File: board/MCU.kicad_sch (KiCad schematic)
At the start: 20 parts, among them Q1 NMOS, U1 1EDL8011XUMA1, U7 ESP32-S2-DEVKITM-1U

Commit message: Add OpAmp link
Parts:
- removed Conn1: Molex_uF_D_10, MRDT_Connectors:MOLEX_uF_D_10_Horizontal, symbol MRDT_Connectors:Molex_uF_D_10
- added Conn5: Molex_SL_09, symbol MRDT_Connectors:Molex_SL_09
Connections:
- net +5V: now also Conn5.8
- net GND: now also Conn5.7
- net GPIO 10: now also Conn5.1
- net GPIO 4: now also Conn5.9
- net GPIO 5: now also Conn5.6
- net GPIO 6: now also Conn5.5
- net GPIO 7: now also Conn5.4
- net GPIO 8: now also Conn5.3
- net GPIO 9: now also Conn5.2
- no-connect marks 0 -> 1
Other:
- moved on the sheet: Q1
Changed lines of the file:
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@@
 	)
 	(junction
+		(at 123.19 180.34)
+		(diameter 0)
+		(color 0 0 0 0)
+	)
+	(junction
 		(at 123.19 139.7)
 		(diameter 0)
@@
 	)
 	(junction
-		(at 137.16 180.34)
-		(diameter 0)
-		(color 0 0 0 0)
-	)
-	(junction
 		(at 101.6 158.75)
 		(diameter 0)
@@
 		(color 0 0 0 0)
 	)
+	(no_connect
+		(at 157.48 130.81)
+	)
 	(wire
 		(pts
@@
 	(wire
 		(pts
-			(xy 137.16 168.91) (xy 137.16 139.7)
+			(xy 123.19 168.91) (xy 123.19 139.7)
 		)
 		(stroke
@@
 	(wire
 		(pts
-			(xy 101.6 173.99) (xy 129.54 173.99)
+			(xy 101.6 173.99) (xy 115.57 173.99)
 		)
 		(stroke
@@
 	(wire
 		(pts
-			(xy 114.3 180.34) (xy 137.16 180.34)
-		)
-		(stroke
-			(width 0)
-			(type default)
-		)
-	)
-	(wire
-		(pts
-			(xy 137.16 139.7) (xy 123.19 139.7)
+			(xy 114.3 180.34) (xy 123.19 180.34)
 		)
 		(stroke
@@
 	(wire
 		(pts
-			(xy 137.16 180.34) (xy 137.16 184.15)
+			(xy 123.19 180.34) (xy 123.19 184.15)
 		)
 		(stroke
@@
 	(wire
 		(pts
-			(xy 137.16 180.34) (xy 137.16 179.07)
+			(xy 123.19 180.34) (xy 123.19 179.07)
 		)
 		(stroke
@@
 	(wire
 		(pts
-			(xy 101.6 172.72) (xy 101.6 173.99)
+			(xy 101.6 173.99) (xy 101.6 172.72)
 		)
 		(stroke
@@
 	(global_label "ESC_PWR"
 		(shape output)
-		(at 137.16 184.15 270)
+		(at 123.19 184.15 270)
 		(fields_autoplaced yes)
 		(effects
@@
 		)
 		(property "Intersheetrefs" "${INTERSHEET_REFS}"
-			(at 137.16 195.7227 90)
+			(at 123.19 195.7227 90)
 			(effects
 				(font
@@
 	(symbol
 		(lib_id "Simulation_SPICE:NMOS")
-		(at 134.62 173.99 0)
+		(at 120.65 173.99 0)
 		(unit 1)
 		(exclude_from_sim no)
@@
 		(fields_autoplaced yes)
 		(property "Reference" "Q1"
-			(at 140.97 172.7199 0)
+			(at 127 172.7199 0)
 			(effects
 				(font
@@
 		)
 		(property "Value" "NMOS"
-			(at 140.97 175.2599 0)
+			(at 127 175.2599 0)
 			(effects
 				(font
@@
 		)
 		(property "Footprint" ""
-			(at 139.7 171.45 0)
+			(at 125.73 171.45 0)
 			(effects
 				(font
@@
 		)
 		(property "Datasheet" "https://ngspice.sourceforge.io/docs/ngspice-html-manual/manual.xhtml#cha_MOSFETs"
-			(at 134.62 186.69 0)
+			(at 120.65 186.69 0)
 			(effects
 				(font
@@
 		)
 		(property "Description" "N-MOSFET transistor, drain/source/gate"
-			(at 134.62 173.99 0)
+			(at 120.65 173.99 0)
 			(effects
 				(font
@@
 		)
 		(property "Sim.Device" "NMOS"
-			(at 134.62 191.135 0)
+			(at 120.65 191.135 0)
 			(effects
 				(font
@@
 		)
 		(property "Sim.Type" "VDMOS"
-			(at 134.62 193.04 0)
+			(at 120.65 193.04 0)
 			(effects
 				(font
@@
 		)
 		(property "Sim.Pins" "1=D 2=G 3=S"
-			(at 134.62 189.23 0)
+			(at 120.65 189.23 0)
 			(effects
 				(font
@@
 	)
 	(symbol
+		(lib_id "MRDT_Connectors:Molex_SL_09")
+		(at 33.02 39.37 180)
+		(unit 1)
+		(exclude_from_sim no)
+		(in_bom yes)
+		(on_board yes)
+		(dnp no)
+		(fields_autoplaced yes)
+		(property "Reference" "Conn5"
+			(at 31.75 34.29 0)
+			(effects
+				(font
+					(size 1.524 1.524)
+				)
+			)
+		)
+		(property "Value" "Molex_SL_09"
+			(at 31.75 36.83 0)
+			(effects
+				(font
+					(size 1.524 1.524)
+				)
+			)
+		)
+		(property "Footprint" ""
+			(at 33.02 49.53 0)
+			(effects
+				(font
+					(size 1.524 1.524)
+				)
+				(hide yes)
+			)
+		)
+		(property "Datasheet" ""
+			(at 33.02 49.53 0)
+			(effects
+				(font
+					(size 1.524 1.524)
+				)
+				(hide yes)
+			)
+		)
+		(property "Description" ""
+			(at 33.02 39.37 0)
+			(effects
+				(font
+					(size 1.27 1.27)
+				)
+				(hide yes)
+			)
+		)
+		(pin "2"
+		)
+		(pin "5"
+		)
+		(pin "4"
+		)
+		(pin "1"
+		)
+		(pin "3"
+		)
+		(pin "8"
+		)
+		(pin "6"
+		)
+		(pin "9"
+		)
+		(pin "7"
+		)
+		(instances
+			(project ""
+				(path "/fbd9c71c-f200-4aab-a303-9f269bc9de13/790be9a8-4a0a-446c-a87f-40bdf4df72de"
+					(reference "Conn5")
+					(unit 1)
+				)
+			)
+		)
+	)
+	(symbol
 		(lib_id "power:GND")
 		(at 96.52 173.99 0)
@@
 					(unit 1)
 				)
-			)
-		)
-	)
-	(symbol
-		(lib_id "MRDT_Connectors:Molex_uF_D_10")
-		(at 33.02 36.83 180)
-		(unit 1)
-		(exclude_from_sim no)
-		(in_bom yes)
-		(on_board yes)
-		(dnp no)
-		(fields_autoplaced yes)
-		(property "Reference" "Conn1"
-			(at 31.75 31.75 0)
-			(effects
-				(font
-					(size 1.524 1.524)
-				)
-			)
-		)
-		(property "Value" "Molex_uF_D_10"
-			(at 31.75 34.29 0)
-			(effects
-				(font
-					(size 1.524 1.524)
-				)
-			)
-		)
-		(property "Footprint" "MRDT_Connectors:MOLEX_uF_D_10_Horizontal"
-			(at 33.02 49.53 0)
-			(effects
-				(font
-					(size 1.524 1.524)
-				)
-				(hide yes)
-			)
-		)
-		(property "Datasheet" ""
-			(at 33.02 49.53 0)
-			(effects
-				(font
-					(size 1.524 1.524)
-				)
-				(hide yes)
-			)
-		)
-		(property "Description" ""
-			(at 33.02 36.83 0)
-			(effects
-				(font
-					(size 1.27 1.27)
-				)
-				(hide yes)
-			)
-		)
-		(pin "7"
-		)
-		(pin "9"
-		)
-		(pin "1"
-		)
-		(pin "5"
-		)
-		(pin "6"
-		)
-		(pin "2"
-		)
-		(pin "3"
-		)
-		(pin "4"
-		)
-		(pin "8"
-		)
-		(pin "10"
-		)
-		(instances
-			(project ""
-				(path "/fbd9c71c-f200-4aab-a303-9f269bc9de13/790be9a8-4a0a-446c-a87f-40bdf4df72de"
-					(reference "Conn1")
-					(unit 1)
-				)

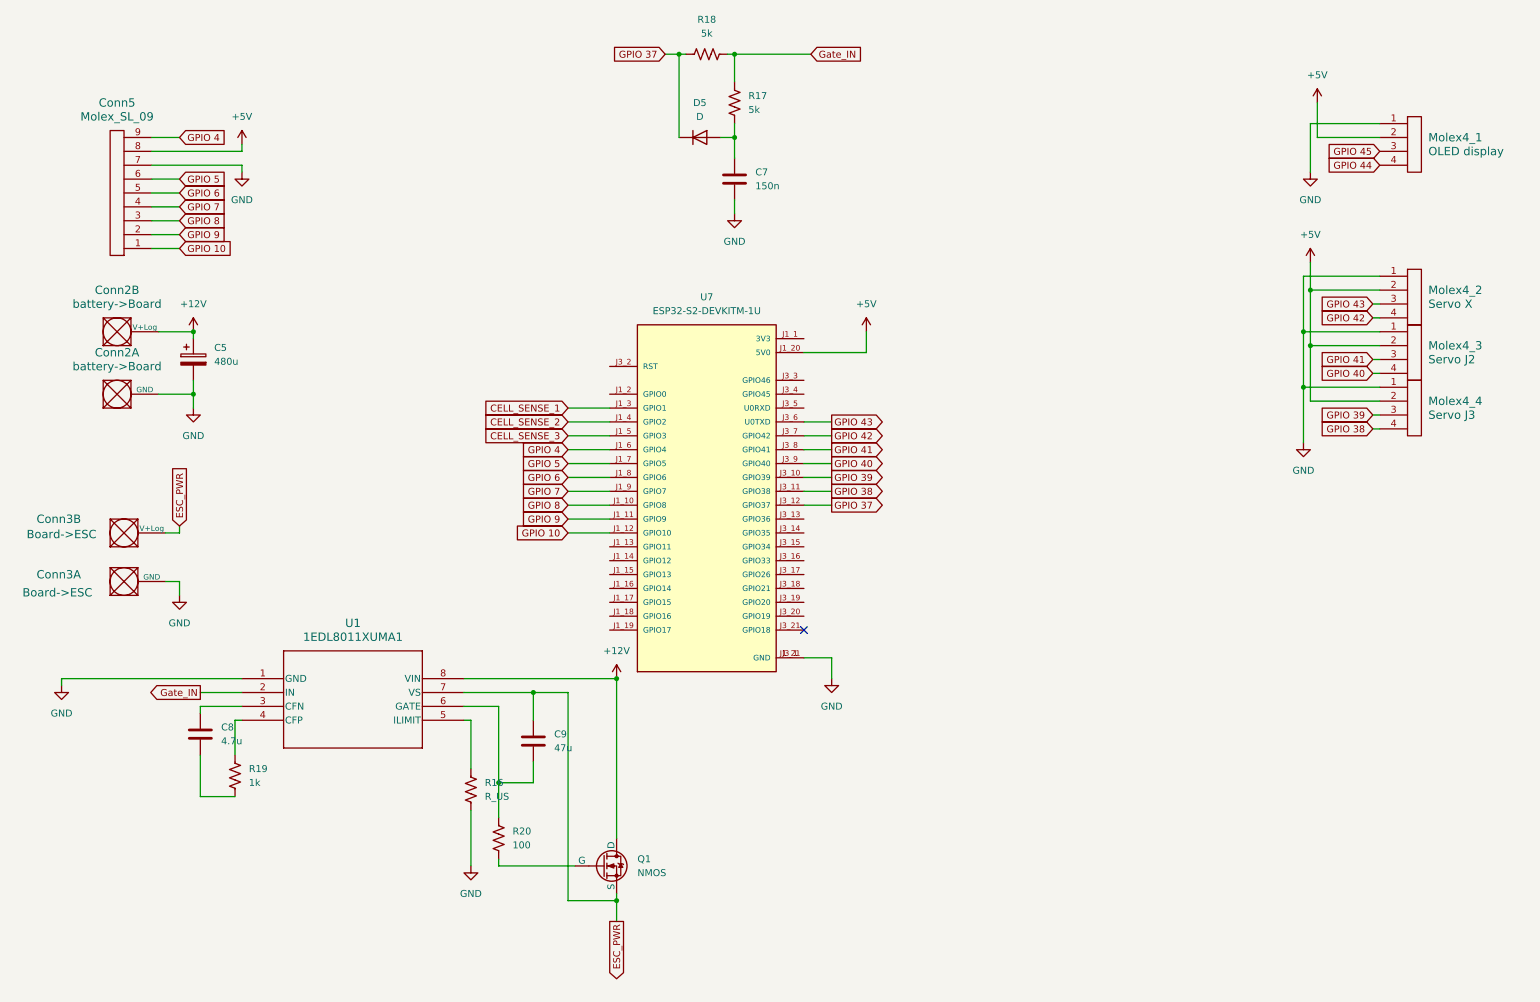
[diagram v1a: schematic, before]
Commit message: Add Debbuger
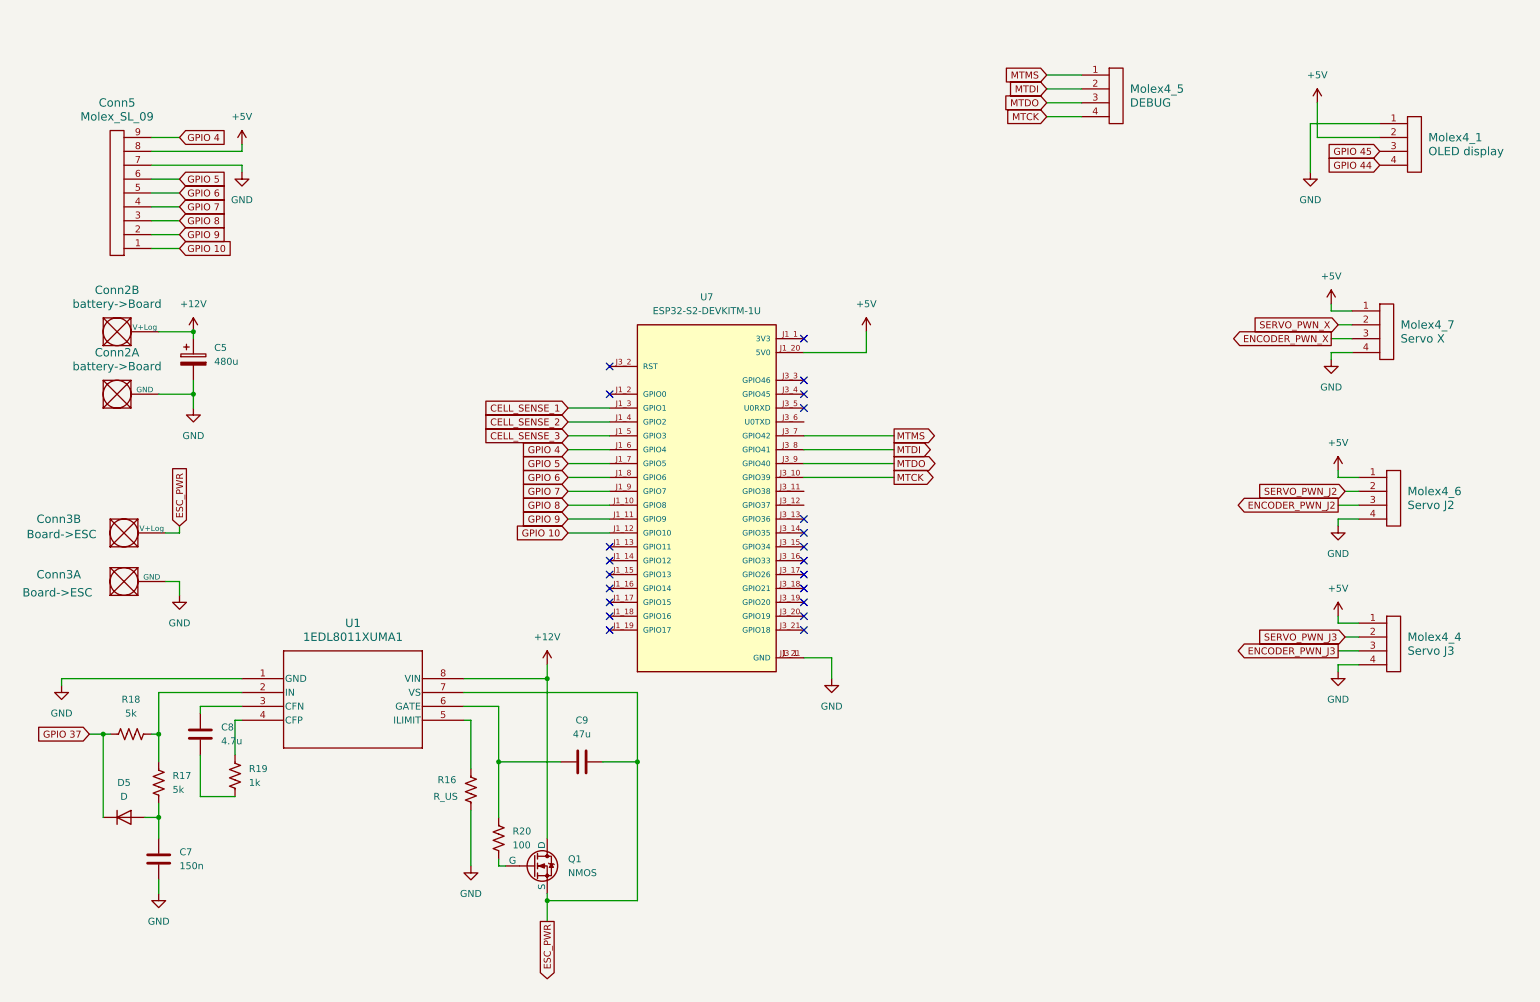
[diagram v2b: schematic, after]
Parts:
- removed Molex4_2: Servo X, symbol MRDT_Connectors:Molex_SL_04
- removed Molex4_3: Servo J2, symbol MRDT_Connectors:Molex_SL_04
- added Molex4_5: DEBUG, symbol MRDT_Connectors:Molex_SL_04
- added Molex4_6: Servo J2, symbol MRDT_Connectors:Molex_SL_04
- added Molex4_7: Servo X, symbol MRDT_Connectors:Molex_SL_04
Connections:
- net +5V: now also Molex4_4.1, Molex4_6.1, Molex4_7.1; no longer Molex4_4.2
- net ESC_PWR: now also C9.2; no longer C9.1
- net GND: now also Molex4_4.4, Molex4_6.4, Molex4_7.4; no longer Molex4_4.1
- net GPIO 37: no longer U7.J3_12 (GPIO37)
- net at R20.1, U1.6 (GATE): now also C9.1; no longer C9.2
- net GPIO 38: no longer names the net of U7.J3_11 (GPIO38)
- net GPIO 38: no longer Molex4_4.4
- net GPIO 39 renamed ENCODER_PWN_J3
- net ENCODER_PWN_J3: no longer U7.J3_10 (GPIO39)
- net GPIO 40 renamed MTDO
- net MTDO: now also Molex4_5.3
- net GPIO 41 renamed MTDI
- net MTDI: now also Molex4_5.2
- net GPIO 42 renamed MTMS
- net MTMS: now also Molex4_5.1
- net GPIO 43: no longer names the net of U7.J3_6 (U0TXD)
- net Gate_IN: no longer names the net of R17.1, R18.2, U1.2 (IN)
- new net ENCODER_PWN_J2: Molex4_6.3
- new net ENCODER_PWN_X: Molex4_7.3
- new net MTCK: Molex4_5.4, U7.J3_10 (GPIO39)
- new net SERVO_PWN_J2: Molex4_6.2
- new net SERVO_PWN_J3: Molex4_4.2
- new net SERVO_PWN_X: Molex4_7.2
- no-connect marks 1 -> 22
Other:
- moved on the sheet: C7, C9, D5, Molex4_4, Q1, R17, R18

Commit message: fixed some review issues and footprints
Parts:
- C5: value 480u -> 480uF; footprint (none) -> Capacitor_SMD:C_0603_1608Metric_Pad1.08x0.95mm_HandSolder
- C7: value 150n -> 150nF; footprint (none) -> Capacitor_SMD:C_0603_1608Metric_Pad1.08x0.95mm_HandSolder
- C8: value 4.7u -> 4.7uF; footprint (none) -> Capacitor_SMD:C_0603_1608Metric_Pad1.08x0.95mm_HandSolder
- C9: value 47u -> 47uF; footprint (none) -> Capacitor_SMD:C_0603_1608Metric_Pad1.08x0.95mm_HandSolder
- Conn2, Conn3: footprint (none) -> MRDT_Connectors:Anderson_2_Horizontal_Side_by_Side
- Conn5, Molex4_1, Molex4_4, Molex4_5, Molex4_6, Molex4_7: footprint (none) -> MRDT_Connectors:MOLEX_SL_04_Vertical
- D5: footprint (none) -> Diode_SMD:D_0603_1608Metric
- R16, R17, R18, R19, R20: footprint (none) -> Resistor_SMD:R_0603_1608Metric_Pad0.98x0.95mm_HandSolder
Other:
- moved on the sheet: C5, C7, C8, C9, Conn2A, Conn2B, Conn3A, Conn3B, Conn5, D5, Molex4_6, Molex4_7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

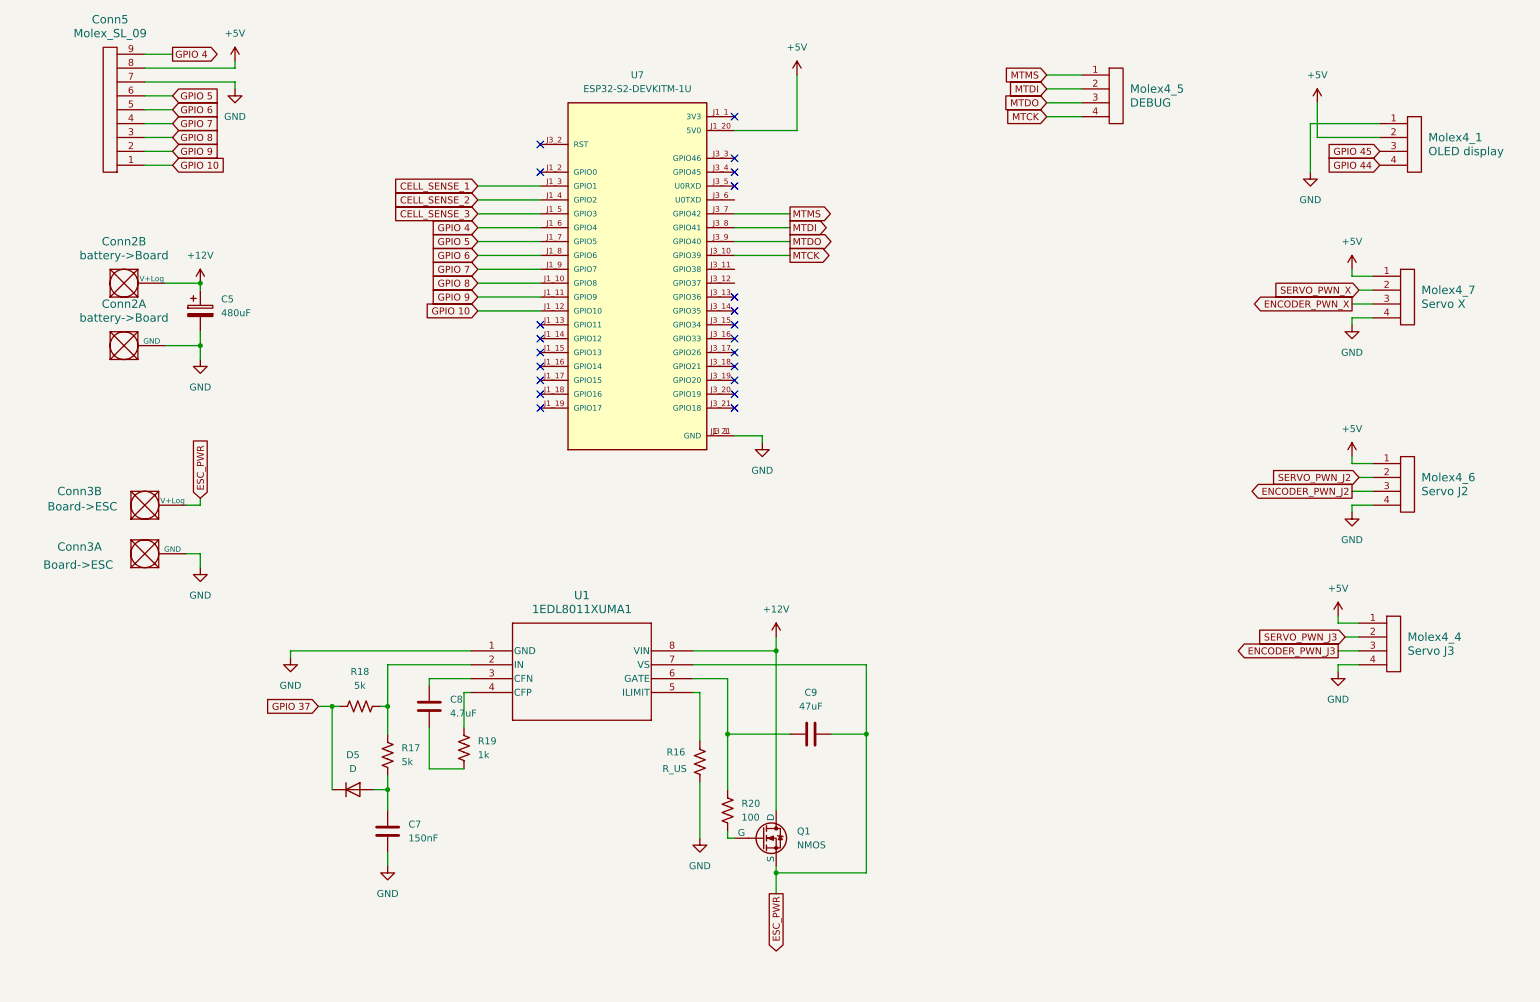
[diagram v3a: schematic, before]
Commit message: Change Gate Driver and Op amp
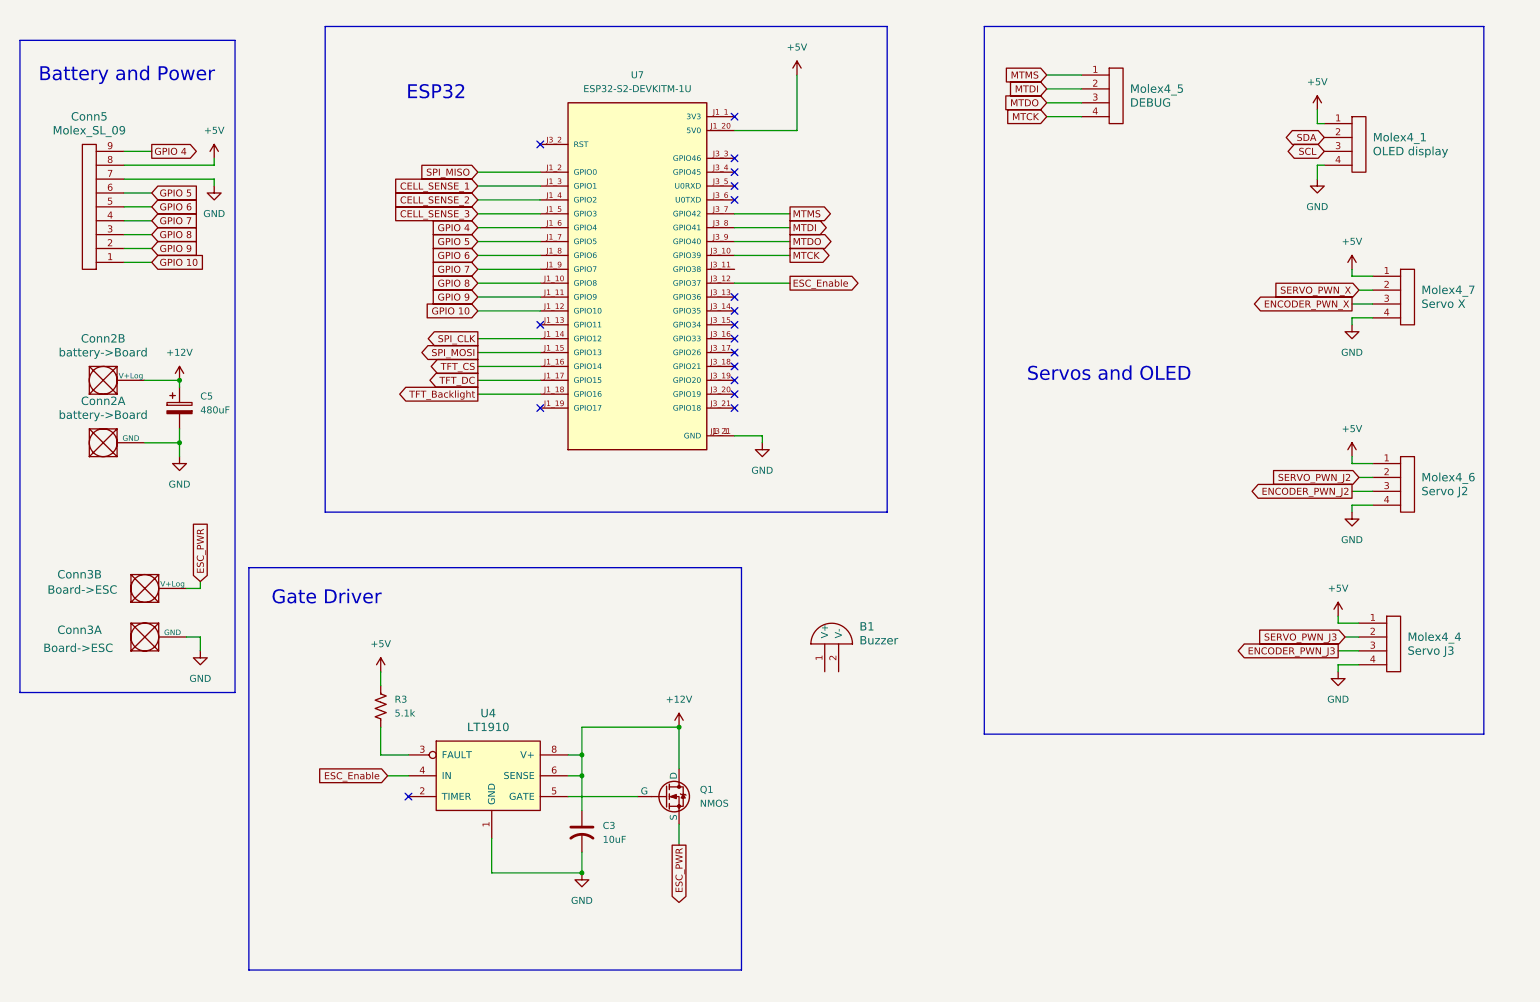
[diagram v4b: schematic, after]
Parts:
- removed C7: 150nF, Capacitor_SMD:C_0603_1608Metric_Pad1.08x0.95mm_HandSolder, symbol Device:C
- removed C8: 4.7uF, Capacitor_SMD:C_0603_1608Metric_Pad1.08x0.95mm_HandSolder, symbol Device:C
- removed C9: 47uF, Capacitor_SMD:C_0603_1608Metric_Pad1.08x0.95mm_HandSolder, symbol Device:C
- removed D5: D, Diode_SMD:D_0603_1608Metric, symbol Device:D
- removed R16: R_US, Resistor_SMD:R_0603_1608Metric_Pad0.98x0.95mm_HandSolder, symbol Device:R_US
- removed R17, R18: 5k, Resistor_SMD:R_0603_1608Metric_Pad0.98x0.95mm_HandSolder, symbol Device:R_US
- removed R19: 1k, Resistor_SMD:R_0603_1608Metric_Pad0.98x0.95mm_HandSolder, symbol Device:R_US
- removed R20: 100, Resistor_SMD:R_0603_1608Metric_Pad0.98x0.95mm_HandSolder, symbol Device:R_US
- removed U1: 1EDL8011XUMA1, PG-DSO-8-92_INF, symbol MRDT_Devices:1EDL8011XUMA1
- added B1: Buzzer, symbol MRDT_Devices:Buzzer
- added C3: 10uF, symbol Device:C_US
- added R3: 5.1k, symbol Device:R_US
- added U4: LT1910, symbol MRDT_ICs:LT1910
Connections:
- net GPIO 44 is gone; now on net GND: Molex4_1.4
- net +12V: now also C3.1, U4.6 (SENSE), U4.8 (V+)
- net +5V: now also Molex4_1.1, R3.1; no longer Molex4_1.2
- net GND: now also C3.2, U4.1 (GND); no longer Molex4_1.1
- net at Q1.2 (G): now also U4.5 (GATE)
- net SPI_CLK: now reaches U7.J1_14 (GPIO12)
- net SPI_MOSI: now reaches U7.J1_15 (GPIO13)
- net TFT_CS: now reaches U7.J1_16 (GPIO14)
- net TFT_DC: now reaches U7.J1_17 (GPIO15)
- net TFT_Backlight: now reaches U7.J1_18 (GPIO16)
- net SPI_MISO: now reaches U7.J1_2 (GPIO0)
- net ESC_Enable: now reaches U7.J3_12 (GPIO37)
- net ESC_Enable: now also U4.4 (IN)
- net GPIO 45 renamed SCL
- new net: R3.2, U4.3 (FAULT)
- new net SDA: Molex4_1.2
- no-connect marks 22 -> 18
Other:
- note added: "Battery and Power"
- note added: "ESP32"
- note added: "Gate Driver"
- note added: "Servos and OLED"
- moved on the sheet: C5, Conn2A, Conn2B, Conn3A, Conn3B, Conn5, Molex4_1, Q1
